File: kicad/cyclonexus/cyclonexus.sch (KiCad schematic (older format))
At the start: 19 parts, among them J1 RJ14, J10 RJ14, J11 RJ14, J12 RJ14, J13 RJ14, J14 RJ14, J15 RJ14, J16 RJ14, J17 USB_1, J2 RJ14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

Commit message: various changes to schematics
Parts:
- removed P1: CONN_2, symbol CONN_2
- added C?: 10mf, ~, symbol C
- added CON? (x2): BARREL_JACK, symbol BARREL_JACK
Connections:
- net labels added: +5V
- net labels removed: LED+5V, LEDGND
- wire segments 164 -> 124
- no-connect marks 40 -> 56
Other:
- note added: ".1 mf between all power and gnd? or op-amp circuit makes unecessary?"
- note added: "10mf enough?"
- note added: "connect GND to shield?"
- note added: "connect both to gnd?"
- note added: "second barrel connector, daisy chain to power 2 boards \nand ARM computer"
- note added: "usb power to pi - use square plug for micro-usb cable use"
- moved on the sheet: J1, J10, J11, J12, J13, J14, J15, J16, J17, J2, J3, J4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

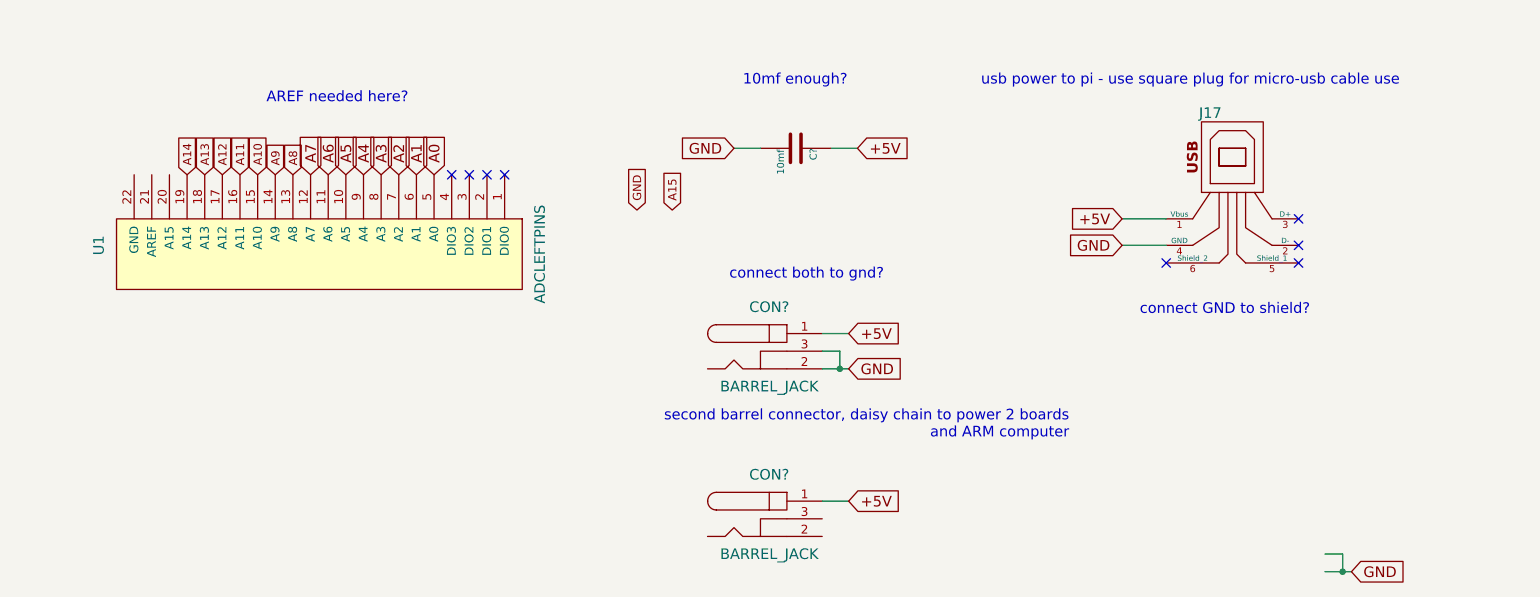
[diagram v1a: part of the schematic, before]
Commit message: updating basic cyclo-sensor.  Still need to verify with actual cyclophone.
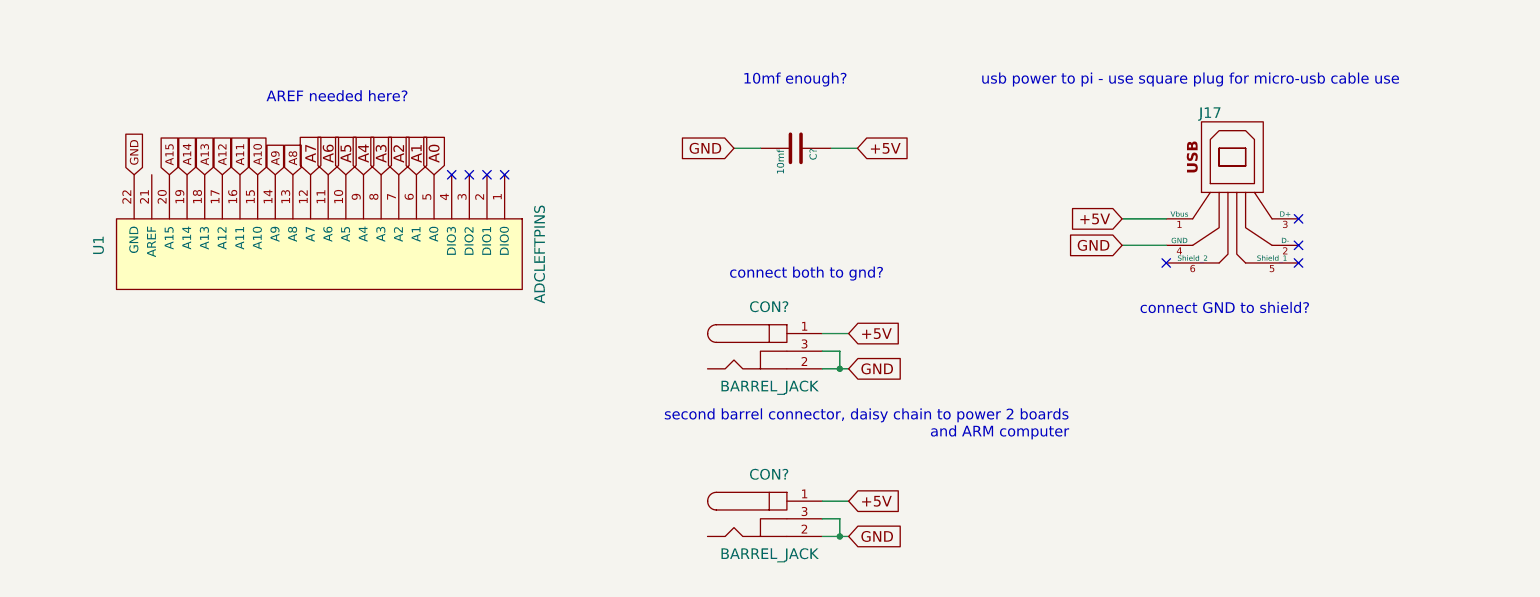
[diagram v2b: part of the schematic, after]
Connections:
- net A15: now also U1.20 (A15)
- net GND: now also CON?.2, CON?.3, U1.22 (GND)
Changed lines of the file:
@@
 Sheet 1 1
 Title ""
-Date "5 apr 2014"
+Date "6 apr 2014"
 Rev ""
 Comp ""
@@
 Text GLabel 5250 5550 1    47   Input ~ 0
 A14
-Text GLabel 8000 5750 1    47   Input ~ 0
+Text GLabel 5150 5550 1    47   Input ~ 0
 A15
-Text GLabel 7800 5750 1    47   Input ~ 0
+Text GLabel 4950 5550 1    47   Input ~ 0
 GND
 Text GLabel 10550 5950 0    60   Input ~ 0
@@
 Text GLabel 9000 7400 2    60   Input ~ 0
 +5V
-Text GLabel 11850 7800 2    60   Input ~ 0
-GND
-Wire Wire Line
-	11700 7800 11850 7800
-Wire Wire Line
-	11700 7700 11800 7700
-Wire Wire Line
-	11800 7700 11800 7800
-Connection ~ 11800 7800
 Wire Wire Line
 	8850 7400 9000 7400
@@
 Text Notes 10650 6350 0    60   ~ 0
 connect GND to shield?
+Text GLabel 9000 7600 2    60   Input ~ 0
+GND
+Wire Wire Line
+	8850 7600 9000 7600
+Wire Wire Line
+	8850 7500 8950 7500
+Wire Wire Line
+	8950 7500 8950 7600
+Connection ~ 8950 7600
 $EndSCHEMATC

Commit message: various changes!  notes frm Dan.
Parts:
- C?: value 10mf -> 10uf
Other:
- note added: "put 2500uf if anything."
- note removed: ".1 mf between all power and gnd? or op-amp circuit makes unecessary?"
- note removed: "10mf enough?"
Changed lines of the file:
@@
 Sheet 1 1
 Title ""
-Date "6 apr 2014"
+Date "9 apr 2014"
 Rev ""
 Comp ""
@@
 P 8700 5400
 F 0 "C?" H 8700 5500 40  0000 L CNN
-F 1 "10mf" H 8706 5315 40  0000 L CNN
+F 1 "10uf" H 8706 5315 40  0000 L CNN
 F 2 "~" H 8738 5250 30  0000 C CNN
 F 3 "~" H 8700 5400 60  0000 C CNN
@@
 Wire Wire Line
 	8350 5400 8500 5400
-Text Notes 8400 5050 0    60   ~ 0
-10mf enough?
-Text Notes 6650 4500 0    60   ~ 0
-.1 mf between all power and gnd?  or op-amp circuit makes unecessary?
+Text Notes 8250 5150 0    60   ~ 0
+put 2500uf if anything.
 $Comp
 L BARREL_JACK CON?

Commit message: remove PI pins, power regulator thingy, add optional DIO connector.
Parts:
- added P1: CONN_4, symbol CONN_4
- U1: value ADCLEFTPINS -> ADCPINS
- gave numbers to parts that had none: 3
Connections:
- net +5V: now also U1.21 (AREF)
- net D0: now reaches U1.1 (DIO0)
- net D0: now also P1.1 (P1)
- net D1: now reaches U1.2 (DIO1)
- net D1: now also P1.2 (P2)
- net D2: now reaches U1.3 (DIO2)
- net D2: now also P1.3 (P3)
- net D3: now reaches U1.4 (DIO3)
- net D3: now also P1.4 (P4)
- no-connect marks 56 -> 52
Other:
- note added: "optional DIO pins.\nallow for screw terminals."
- note removed: "connect both to gnd?"
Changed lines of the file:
@@
 Sheet 1 1
 Title ""
-Date "9 apr 2014"
+Date "13 apr 2014"
 Rev ""
 Comp ""
@@
 P 6250 6000
 F 0 "U1" H 6200 4500 60  0000 C CNN
-F 1 "ADCLEFTPINS" H 6250 7000 60  0000 C CNN
+F 1 "ADCPINS" H 6250 7000 60  0000 C CNN
 F 2 "" H 6250 6000 60  0001 C CNN
 F 3 "" H 6250 6000 60  0001 C CNN
@@
 Wire Wire Line
 	10800 5950 10550 5950
-NoConn ~ 6750 5550
-NoConn ~ 6850 5550
-NoConn ~ 6950 5550
-NoConn ~ 7050 5550
-Text Notes 5700 5150 0    60   ~ 0
+Text Notes 4650 4950 0    60   ~ 0
 AREF needed here?
 NoConn ~ 14050 3700
@@
 NoConn ~ 3550 3700
 $Comp
-L BARREL_JACK CON?
+L BARREL_JACK CON1
 U 1 1 53402D91
 P 8550 6550
-F 0 "CON?" H 8550 6800 60  0000 C CNN
+F 0 "CON1" H 8550 6800 60  0000 C CNN
 F 1 "BARREL_JACK" H 8550 6350 60  0000 C CNN
 F 2 "" H 8550 6550 60  0000 C CNN
@@
 Wire Wire Line
 	8850 6450 9000 6450
-Text Notes 9200 6150 2    60   ~ 0
-connect both to gnd?
 Text Notes 9750 5050 0    60   ~ 0
 usb power to pi - use square plug for micro-usb cable use
@@
 	8900 5400 9050 5400
 $Comp
-L C C?
+L C C1
 U 1 1 534031B8
 P 8700 5400
-F 0 "C?" H 8700 5500 40  0000 L CNN
+F 0 "C1" H 8700 5500 40  0000 L CNN
 F 1 "10uf" H 8706 5315 40  0000 L CNN
 F 2 "~" H 8738 5250 30  0000 C CNN
@@
 put 2500uf if anything.
 $Comp
-L BARREL_JACK CON?
+L BARREL_JACK CON2
 U 1 1 53403D81
 P 8550 7500
-F 0 "CON?" H 8550 7750 60  0000 C CNN
+F 0 "CON2" H 8550 7750 60  0000 C CNN
 F 1 "BARREL_JACK" H 8550 7300 60  0000 C CNN
 F 2 "" H 8550 7500 60  0000 C CNN
@@
 	8950 7500 8950 7600
 Connection ~ 8950 7600
+Text GLabel 5250 5100 2    47   Input ~ 0
++5V
+Text GLabel 7050 5550 1    43   Input ~ 0
+D0
+Text GLabel 6950 5550 1    43   Input ~ 0
+D1
+Text GLabel 6850 5550 1    43   Input ~ 0
+D2
+Text GLabel 6750 5550 1    43   Input ~ 0
+D3
+$Comp
+L CONN_4 P1
+U 1 1 534AB6FD
+P 5950 7400
+F 0 "P1" V 5900 7400 50  0000 C CNN
+F 1 "CONN_4" V 6000 7400 50  0000 C CNN
+F 2 "" H 5950 7400 60  0000 C CNN
+F 3 "" H 5950 7400 60  0000 C CNN
+	1    5950 7400
+	0    1    1    0
+$EndComp
+Text GLabel 6100 7050 1    43   Input ~ 0
+D0
+Text GLabel 6000 7050 1    43   Input ~ 0
+D1
+Text GLabel 5900 7050 1    43   Input ~ 0
+D2
+Text GLabel 5800 7050 1    43   Input ~ 0
+D3
+Text GLabel 5050 5550 1    47   Input ~ 0
+AREF
+Text GLabel 4950 5100 0    47   Input ~ 0
+AREF
+Wire Wire Line
+	4950 5100 5250 5100
+Text Notes 5400 7700 0    60   ~ 0
+optional DIO pins.\nallow for screw terminals.
 $EndSCHEMATC

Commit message: various changes... pcb files for cyclo-nexus, cyclo-adc.
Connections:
- net GND: now also J17.5 (Shield_1), J17.6 (Shield_2)
- no-connect marks 52 -> 50
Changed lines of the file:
@@
 LIBS:cyclophone-cache
 LIBS:cyclonexus-cache
-EELAYER 27 0
+EELAYER 24 0
 EELAYER END
 $Descr USLedger 17000 11000
@@
 NoConn ~ 11550 5800
 NoConn ~ 11550 5950
-NoConn ~ 11550 6050
-NoConn ~ 10800 6050
 Text GLabel 10550 5800 0    60   Input ~ 0
 +5V
@@
 Text GLabel 5250 5100 2    47   Input ~ 0
 +5V
-Text GLabel 7050 5550 1    43   Input ~ 0
-D0
-Text GLabel 6950 5550 1    43   Input ~ 0
-D1
-Text GLabel 6850 5550 1    43   Input ~ 0
-D2
-Text GLabel 6750 5550 1    43   Input ~ 0
-D3
 $Comp
 L CONN_4 P1
@@
 Text Notes 5400 7700 0    60   ~ 0
 optional DIO pins.\nallow for screw terminals.
+Wire Wire Line
+	10700 5950 10700 6150
+Wire Wire Line
+	10700 6050 10800 6050
+Connection ~ 10700 5950
+Wire Wire Line
+	10700 6150 11550 6150
+Wire Wire Line
+	11550 6150 11550 6050
+Connection ~ 10700 6050
+Text GLabel 7050 5550 1    43   Input ~ 0
+D0
+Text GLabel 6950 5550 1    43   Input ~ 0
+D1
+Text GLabel 6850 5550 1    43   Input ~ 0
+D2
+Text GLabel 6750 5550 1    43   Input ~ 0
+D3
 $EndSCHEMATC
